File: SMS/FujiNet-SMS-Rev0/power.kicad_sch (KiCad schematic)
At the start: 21 parts, among them Q2 AO3401A, U5 AP63203WU, U6 AP2112K-3.3

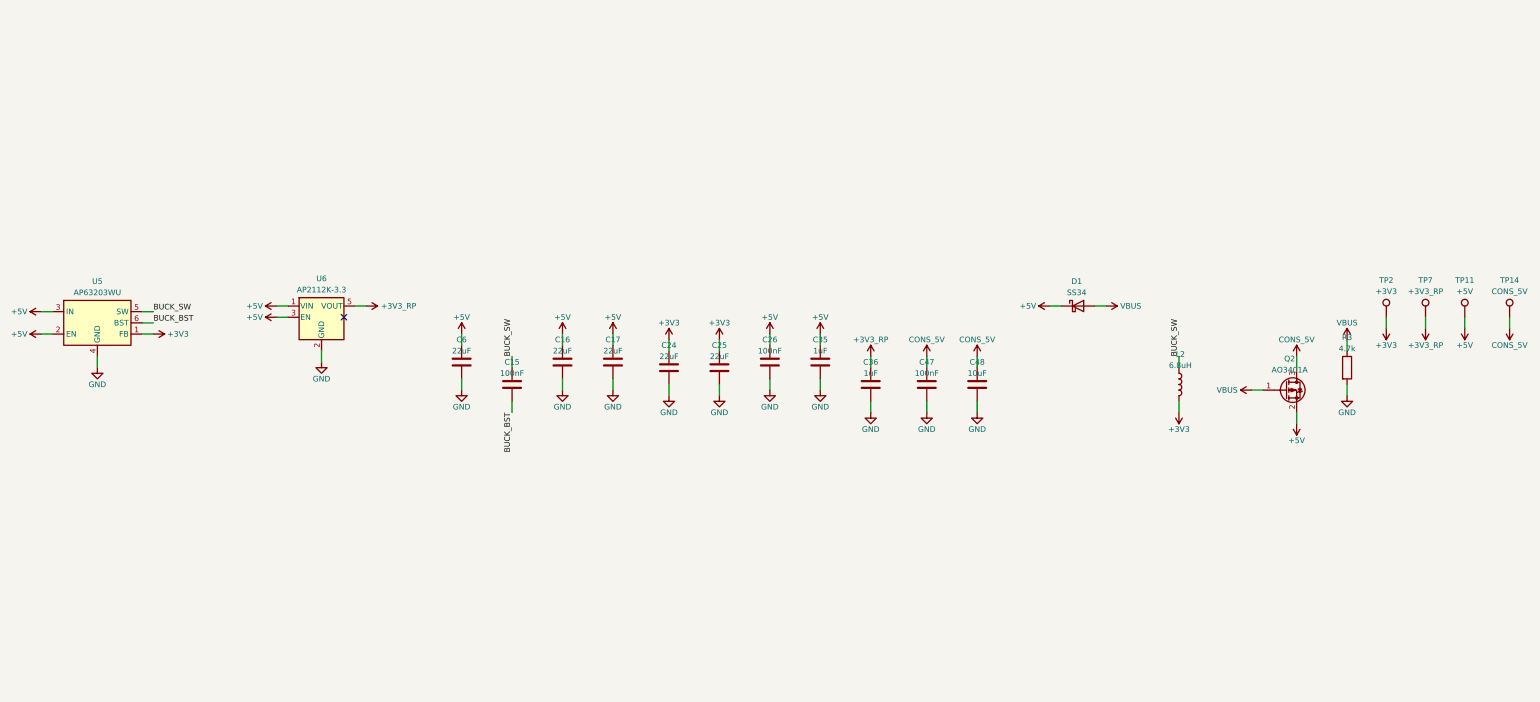
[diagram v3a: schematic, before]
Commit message: SMS Rev0 v2: redraw every sheet to mirror the board
Each sheet is now hand-placed in tools/sch_layout.py from where its parts
sit on the board, turned so the edge fingers face left (south -> left,
north -> right, west -> top, east -> bottom), and every connection on a
sheet is a wire:

- rp-core: the RP2354B core unit with its decoupling ring at the pins, the
  regulator corner, the crystal, SWD, RUN / BOOTSEL and the RESET diode
  (planar).
- fujinet: a functional ESP32-S3 symbol, EN / BOOT, the WS2812, and the
  microSD's SPI lines stepping into the socket with the pull-ups between
  them (planar).
- usb: a functional USB-C symbol, the CP2102N mirrored to face the
  receptacle, and the auto-program pair.  This page has one crossing, which
  cannot be avoided: RTS and DTR sit side by side on the bridge and each
  feeds the base of one transistor and the emitter of the other.
- power: the CONS_5V / VBUS OR on one +5V line, the LDO above it, the buck
  below it, and the rail PWR_FLAGs grouped together (planar).
- root: the board outline at 2:1, turned the same way, with each sheet's
  block at its region and the nine signals between sheets wired without a
  crossing; notes cover the stack-up and the firmware contract.

Gates: gen_sch.py checks the mirror (Kendall tau >= 0.85 per axis for the
major parts, multi-unit packages counted at the centre of their units,
parts within 5 mm on the board counted as level; every sheet is at
1.00 / 1.00) and a crossing budget per sheet (cart-bus 75, usb 1,
others 0).  ERC is 0 at all severities, netlist parity holds, the net
names equal tools/nets.lock, check_nets passes 442/442, check_glue
8192/8192, and edge_orientation passes.

Co-Authored-By: Claude Opus 5.5 <noreply@anthropic.com>
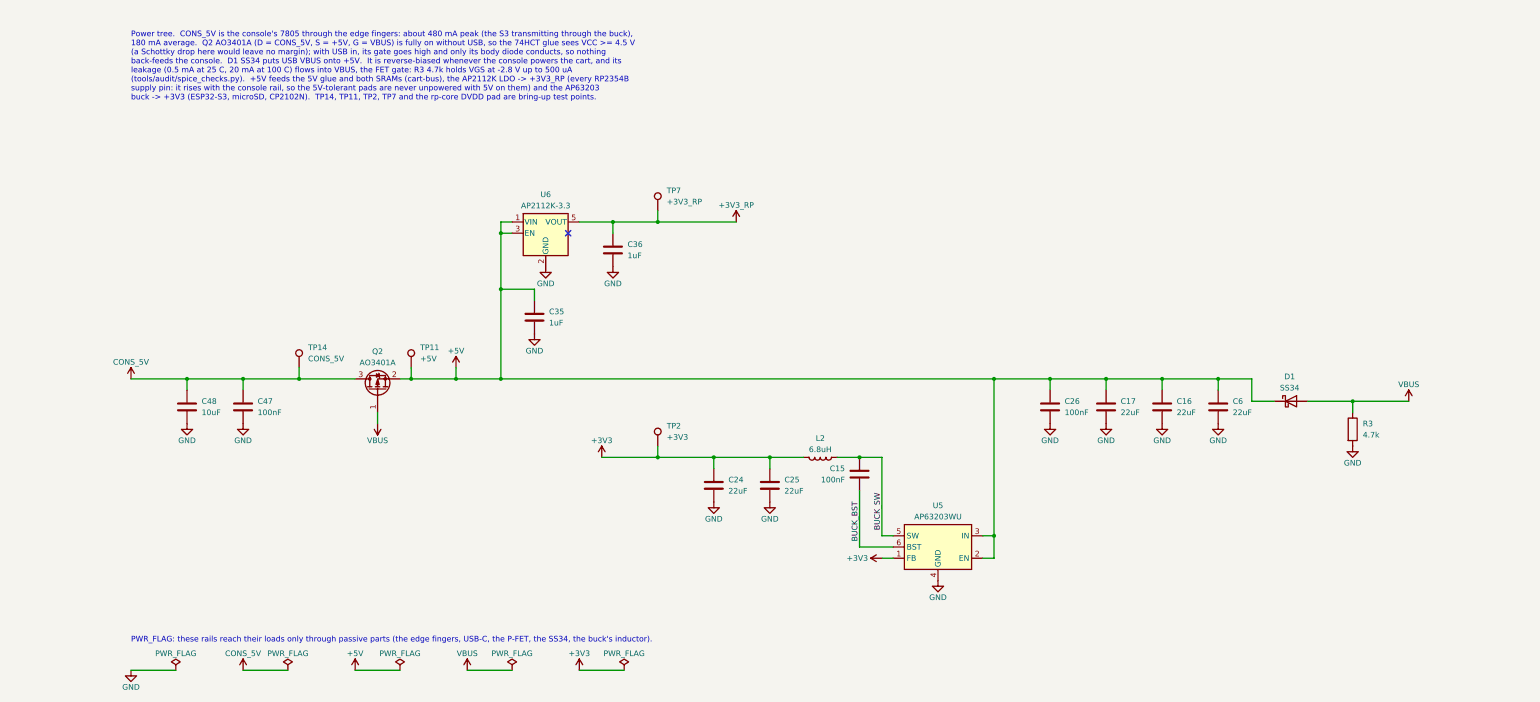
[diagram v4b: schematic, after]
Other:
- note added: "PWR_FLAG: these rails reach their loads only through passive parts (the edge fingers, USB-C, the P-FET, the SS34, the buck's inductor)."
- note added: "Power tree. CONS_5V is the console's 7805 through the edge fingers: about 480 mA peak (the S3 transmitting through the buck), 180 mA average. Q2 AO3401A (D = CONS_5V, S = +5V, G = VBUS) is fully on without USB, so the 74HCT glue sees VCC >= 4.5 V (a Schottky drop here would leave no margin); with USB in, its gate goes high and only its body diode conducts, so nothing back-feeds the console. D1 SS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"
- title: FujiNet SMS Rev0 - Power: console 5V / USB OR, 3.3V buck, RP LDO -> FujiNet SMS Rev0 - Power: 5V OR, 3.3V buck, RP LDO
- moved on the sheet: C15, C16, C17, C24, C25, C26, C35, C36, C47, C48, C6, D1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
